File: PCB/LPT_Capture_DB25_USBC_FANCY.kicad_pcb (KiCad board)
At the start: 2 copper layers, 36 x 22.8 mm, 23 parts, among them J1 GSB1C4621DS2HR, J2 DB25P064TXLF, Q1 SL2301S, Q2 SL2301S, U1 FT245RL

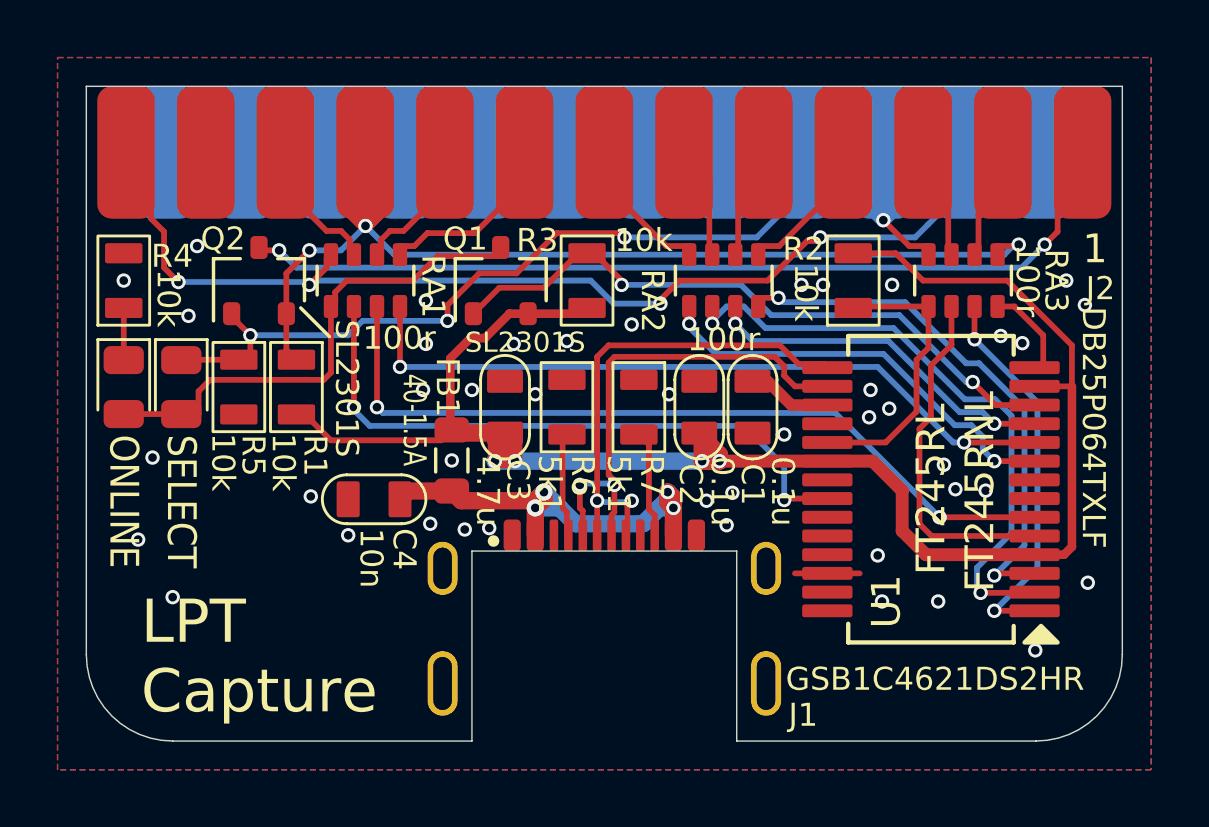
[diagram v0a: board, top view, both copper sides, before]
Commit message: diff pair len match
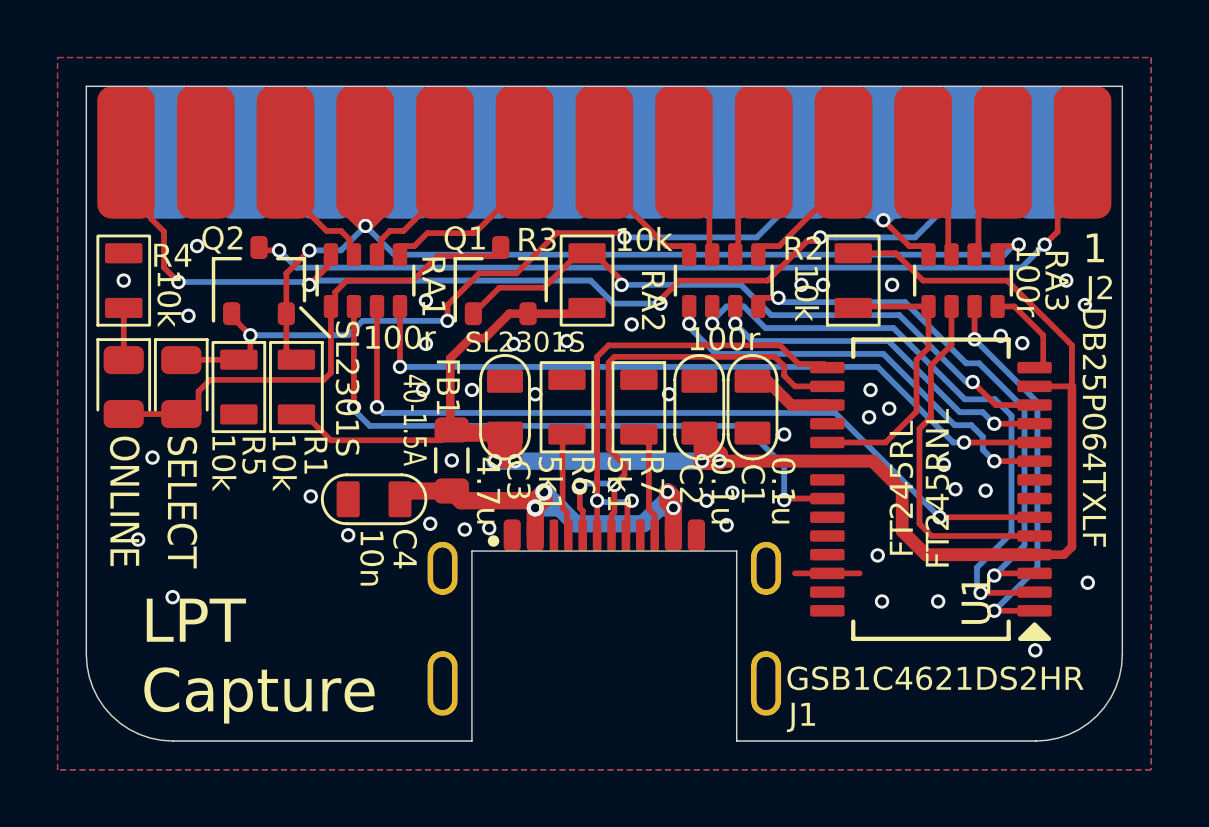
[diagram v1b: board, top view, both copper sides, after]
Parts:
- U1: footprint 000_LOCAL:SSOP-28_5.3x10.2mm_P0.65mm -> 000_LOCAL:SSOP-28

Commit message: db25-usbc-fancy add R8 current limit led when /SELIN driven low
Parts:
- added R8: 10k, 000_LOCAL:R_0805, F.Cu at (135.3, 97.0)
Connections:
- net /pBUSY renamed /BUSY
- net /pD0 renamed /PD0
- net /pD1 renamed /PD1
- net /pD2 renamed /PD2
- net /pD3 renamed /PD3
- net /pD4 renamed /PD4
- net /pD5 renamed /PD5
- net /pD6 renamed /PD6
- net /pD7 renamed /PD7
- net /~{pAUTOF} renamed /~{AUTOF}
- net /~{pRESET} renamed /~{INIT}
- J2 pad 1: /~{pSTROBE} -> /~{STROBE}
- J2 pad 10: /~{STROBE} -> /~{STR}
- J2 pad 13: /pONLINE -> /ONLINE
- J2 pad 15: /pONLINE -> /ONLINE
- J2 pad 17: /~{pSELIN} -> /~{SELIN}
- LED1 pad 2: /ONLINE -> /ON
- LED2 pad 1: /~{pSELIN} -> Net-(LED2-K)
- LED2 pad 2: /ONLINE -> /ON
- Q1 pad 3: /ONLINE -> /ON
- Q2 pad 1: /~{pSELIN} -> /~{SELIN}
- Q2 pad 2: /~{STROBE} -> /~{STR}
- Q2 pad 3: /~{pSTROBE} -> /~{STROBE}
- R1 pad 1: /~{STROBE} -> /~{STR}
- R5 pad 1: /~{pSELIN} -> /~{SELIN}
- RA1 pad 1: /ONLINE -> /ON
- RA1 pad 8: /pONLINE -> /ONLINE
- RA3 pad 5: /~{STROBE} -> /~{STR}
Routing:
- net /pONLINE: track 37.3 -> 0.00 mm, vias 4 -> 0
- net /~{STR}: track 0.00 -> 33.4 mm, vias 0 -> 3
- net /~{pSTROBE}: track 31.7 -> 0.00 mm, vias 2 -> 0
- net /~{SELIN}: track 0.00 -> 28.4 mm, vias 0 -> 3
- net /~{pSELIN}: track 27.4 -> 0.00 mm, vias 3 -> 0
- net /ONLINE: track 17.7 -> 37.6 mm, vias 0 -> 4
- net /ON: track 0.00 -> 17.7 mm
- net Net-(LED2-K): track 0.00 -> 1.83 mm
- net /~{STROBE}: track 33.4 -> 31.8 mm, vias 3 -> 2
- net /D4: track 21.5 -> 21.0 mm
- net GND: track 22.9 -> 22.4 mm, vias 43 -> 44
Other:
- board text added: "LED1, LED2: ${1d2402ba-b0f1-4368-8c52-94dfebae233b:MPN} HOUSING: ${e31e62e7-9523-48c9-88c9-8276f3149c83:MPN}"
- board text added: "R4: ${55b69257-79be-4b26-963a-95a04a5cd9dc:VALUE} R8: ${42bd1e97-0d1c-4d6d-b9e5-a48b9eeee5c7:VALUE}"
- board text removed: "BACKSHELL: ${e31e62e7-9523-48c9-88c9-8276f3149c83:VALUE}"

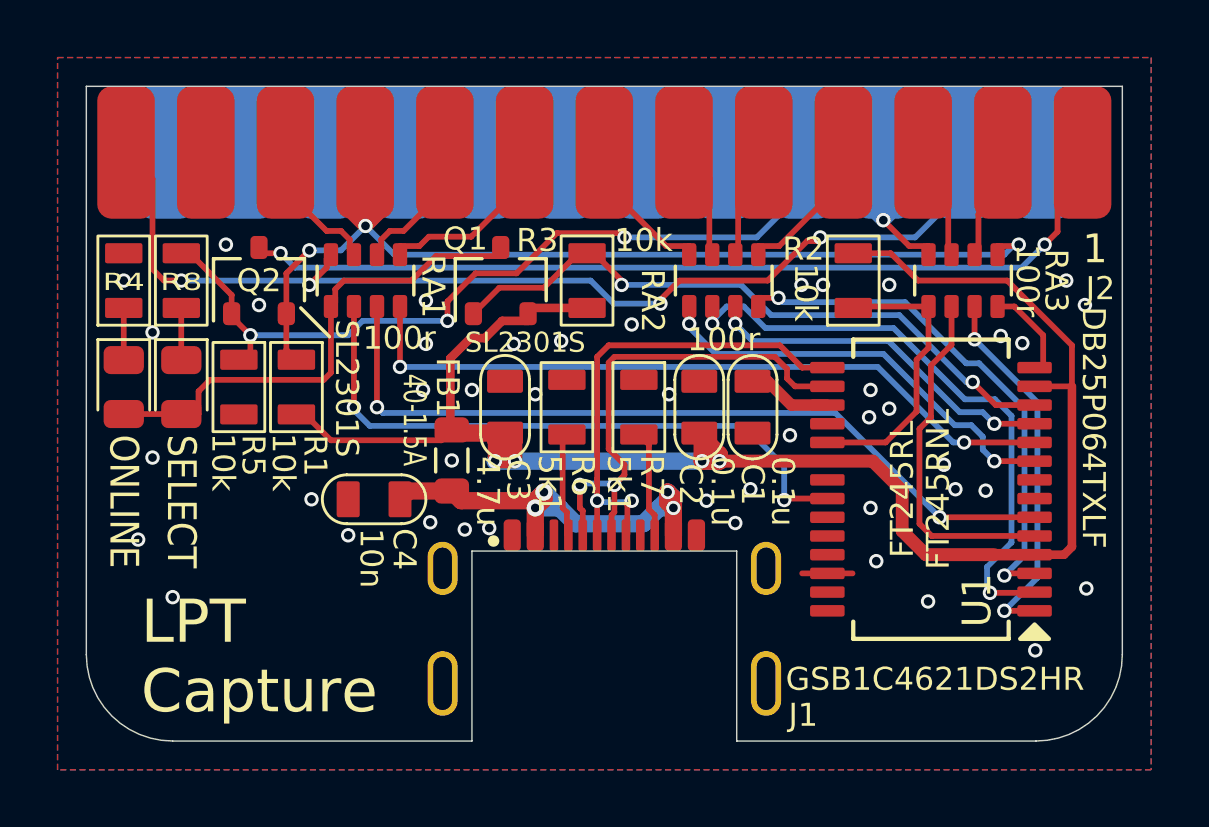
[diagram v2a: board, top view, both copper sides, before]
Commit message: fancy versions - prevent backfeed through online led
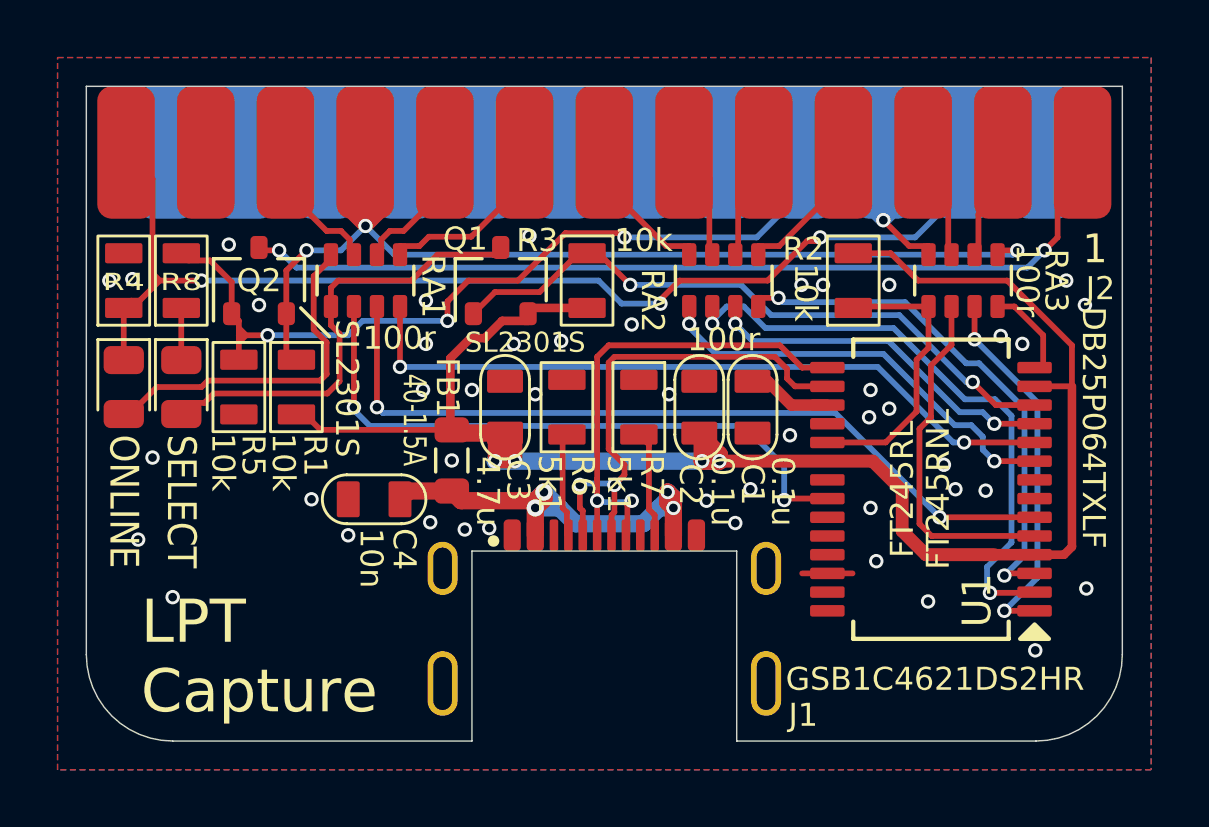
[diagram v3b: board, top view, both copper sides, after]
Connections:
- LED1 pad 1: Net-(LED1-K) -> /ONLINE
- LED1 pad 2: /ON -> Net-(LED1-A)
- R4 pad 1: Net-(LED1-K) -> /ONLINE
- RA1 pad 8: /ONLINE -> Net-(LED1-A)
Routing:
- net Net-(LED1-A): track 0.00 -> 12.2 mm
- net /ONLINE: track 37.6 -> 39.7 mm, vias 4 -> 3
- net /ON: track 17.7 -> 15.8 mm
- net Net-(LED1-K): track 1.81 -> 0.00 mm
- net GND: vias 44 -> 45

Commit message: DB25_USBC_FANCY add reset button
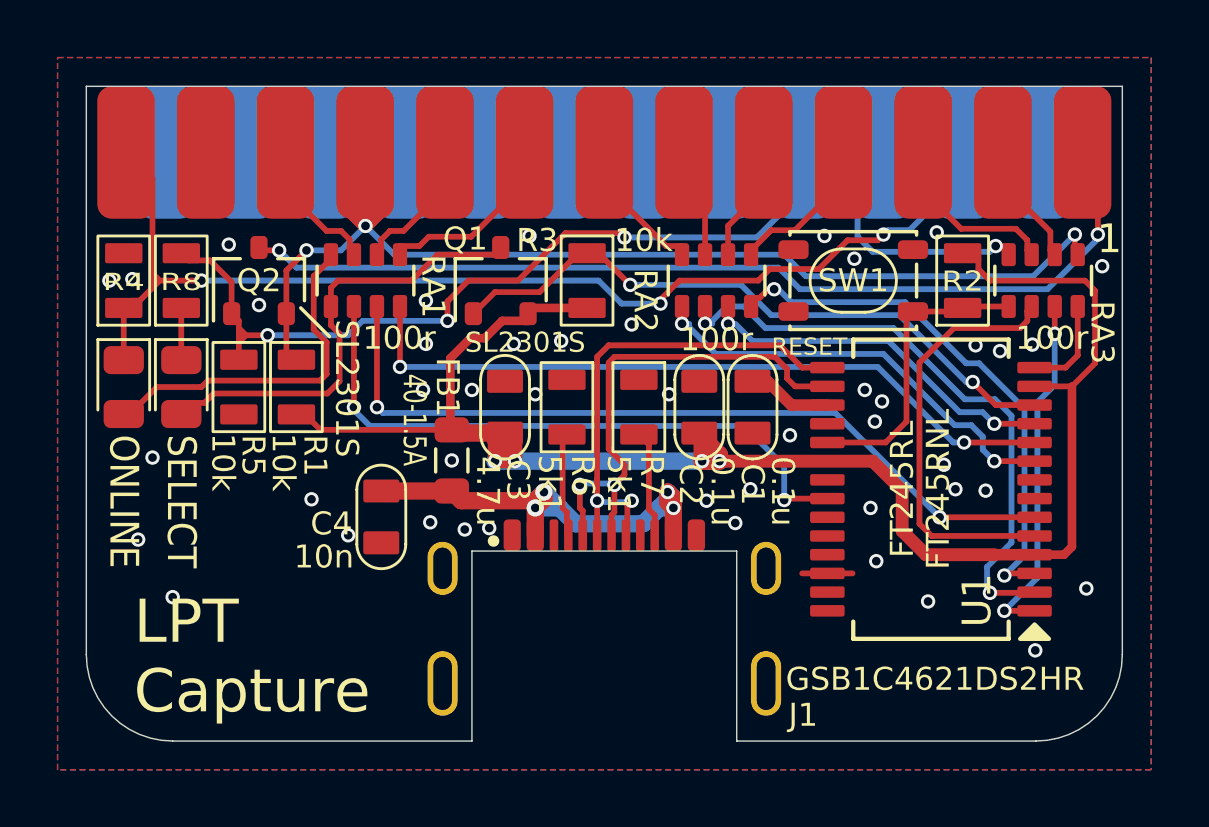
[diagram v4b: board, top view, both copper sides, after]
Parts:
- added SW1: RESET, 000_LOCAL:SW_SPST_PTS810, F.Cu at (158.7, 97.0)
- moved R2 3.80 mm to (162.4, 97.0)
- moved RA3 2.78 mm to (165.2, 97.0)
- moved C4 0.66 mm to (142.2, 105.2), turned to -90 degrees
- moved RA2 0.25 mm to (153.9, 97.0)
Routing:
- net /~{INIT}: track 4.59 -> 9.15 mm
- net /~{STR}: track 33.3 -> 36.1 mm
- net /D1: track 12.2 -> 14.7 mm
- net /PD1: track 3.96 -> 6.22 mm
- net /~{STROBE}: track 31.8 -> 33.7 mm
- net VCC: track 57.9 -> 56.7 mm
- net /D0: track 13.0 -> 12.3 mm
- net VBUS: track 17.5 -> 18.0 mm
- net GND: track 22.4 -> 22.9 mm
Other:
- board text added: "R2: ${a581de28-055e-438c-90cc-f98ef33a464f:VALUE} R4: ${55b69257-79be-4b26-963a-95a04a5cd9dc:VALUE} R8: ${42bd1e97-0d1c-4d6d-b9e5-a48b9eeee5c7:VALUE}"
- board text removed: "R4: ${55b69257-79be-4b26-963a-95a04a5cd9dc:VALUE} R8: ${42bd1e97-0d1c-4d6d-b9e5-a48b9eeee5c7:VALUE}"
